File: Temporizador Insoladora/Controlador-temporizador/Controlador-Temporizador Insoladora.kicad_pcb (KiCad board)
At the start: 2 copper layers, 170.2 x 96.5 mm, 72 parts, among them P1 ICSP, P2 CONN_01X03, P3 CARGA, P4 TRANSF, P5 VAC, P7 CONN_02X08, Q1 BC548, Q2 BC548, Q3 BC548, Q4 BC548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

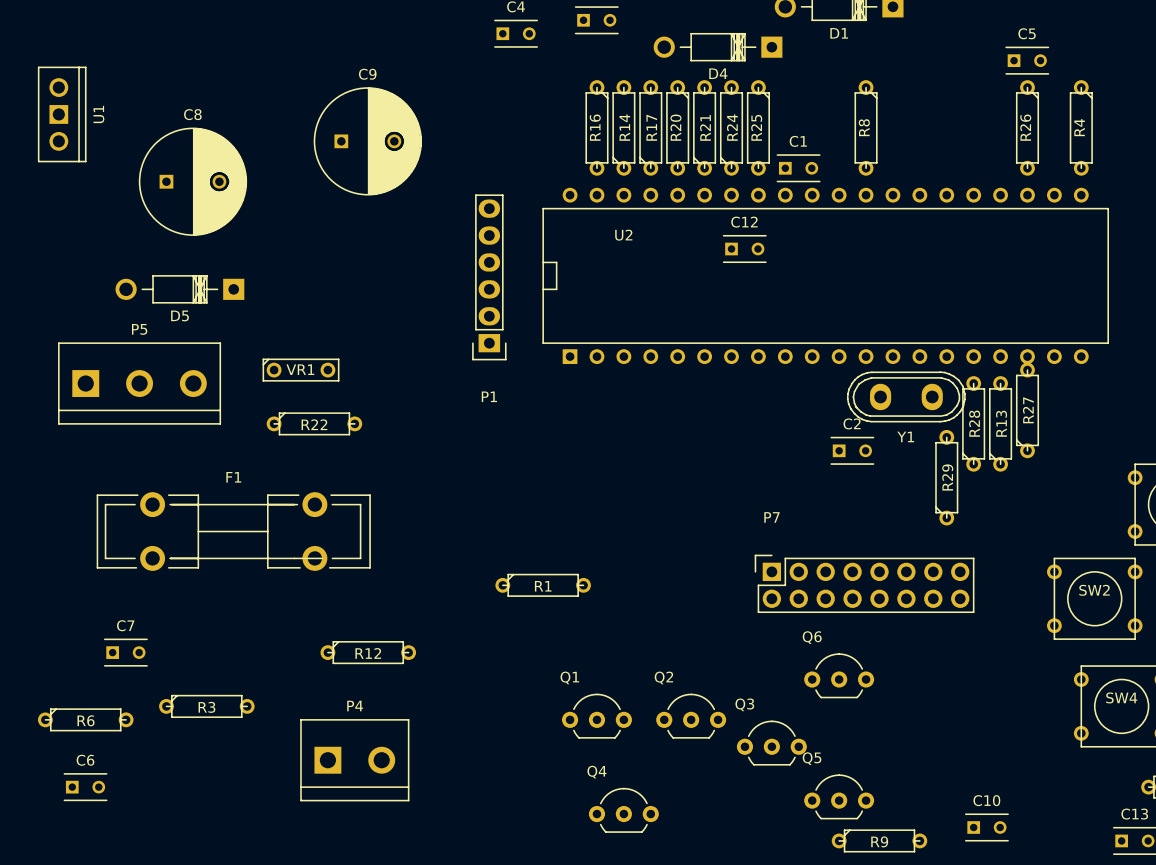
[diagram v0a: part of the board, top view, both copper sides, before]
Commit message: Comienzo a diseñar el controlador
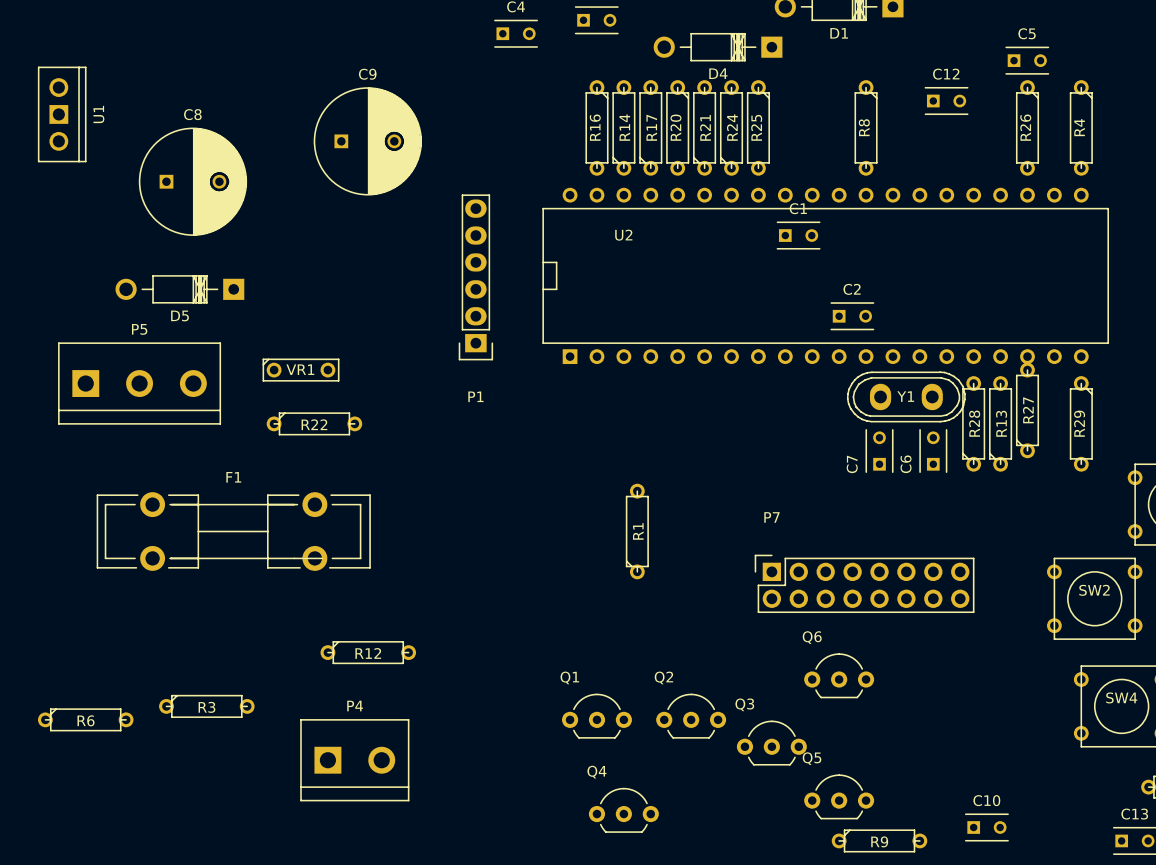
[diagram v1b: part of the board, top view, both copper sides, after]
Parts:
- moved C6 86.8 mm to (143.5, 81.3), turned to 90 degrees
- moved C7 74.5 mm to (138.4, 81.3), turned to 90 degrees
- moved C12 23.6 mm to (143.5, 47.0)
- moved R29 13.7 mm to (157.5, 77.5), turned to 270 degrees
- moved C2 12.7 mm to (134.6, 67.3)
- moved R1 10.2 mm to (115.6, 87.6), turned to 90 degrees
- moved C1 6.35 mm to (129.5, 59.7)
- moved P1 1.27 mm to (100.3, 69.8)
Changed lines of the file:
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@@
     (links 144)
     (no_connects 144)
-    (area 50.749999 22.809999 221.030001 120.315)
+    (area 38.291431 14.93 221.030001 120.315)
     (thickness 1.6)
     (drawings 6)
@@
   )
   (module Capacitors_ThroughHole:C_Rect_L4_W2.5_P2.5 (layer F.Cu)
-    (at 129.54 53.34)
+    (at 129.54 59.69)
     (descr "Film Capacitor Length 4mm x Width 2.5mm, Pitch 2.5mm")
     (tags Capacitor)
@@
   )
   (module Capacitors_ThroughHole:C_Rect_L4_W2.5_P2.5 (layer F.Cu)
-    (at 134.62 80.01)
+    (at 134.62 67.31)
     (descr "Film Capacitor Length 4mm x Width 2.5mm, Pitch 2.5mm")
     (tags Capacitor)
@@
   )
   (module Capacitors_ThroughHole:C_Rect_L4_W2.5_P2.5 (layer F.Cu)
-    (at 62.23 111.76)
+    (at 143.51 81.28 90)
     (descr "Film Capacitor Length 4mm x Width 2.5mm, Pitch 2.5mm")
     (tags Capacitor)
-    (fp_text reference C6 (at 1.25 -2.5) (layer F.SilkS)
-      (effects (font (size 1 1) (thickness 0.15)))
-    )
-    (fp_text value 20pF (at 1.25 2.5) (layer F.Fab)
+    (fp_text reference C6 (at 0 -2.54 90) (layer F.SilkS)
+      (effects (font (size 1 1) (thickness 0.15)))
+    )
+    (fp_text value 20pF (at 2.54 -2.54 90) (layer F.Fab)
       (effects (font (size 1 1) (thickness 0.15)))
     )
@@
     (fp_line (start -0.75 -1.25) (end 3.25 -1.25) (layer F.SilkS) (width 0.15))
     (fp_line (start -0.75 1.25) (end 3.25 1.25) (layer F.SilkS) (width 0.15))
-    (pad 1 thru_hole rect (at 0 0) (size 1.2 1.2) (drill 0.7) (layers *.Cu *.Mask F.SilkS)
-      (net 2 GND))
-    (pad 2 thru_hole circle (at 2.5 0) (size 1.2 1.2) (drill 0.7) (layers *.Cu *.Mask F.SilkS)
+    (pad 1 thru_hole rect (at 0 0 90) (size 1.2 1.2) (drill 0.7) (layers *.Cu *.Mask F.SilkS)
+      (net 2 GND))
+    (pad 2 thru_hole circle (at 2.5 0 90) (size 1.2 1.2) (drill 0.7) (layers *.Cu *.Mask F.SilkS)
       (net 4 "Net-(C6-Pad2)"))
   )
   (module Capacitors_ThroughHole:C_Rect_L4_W2.5_P2.5 (layer F.Cu)
-    (at 66.04 99.06)
+    (at 138.43 81.28 90)
     (descr "Film Capacitor Length 4mm x Width 2.5mm, Pitch 2.5mm")
     (tags Capacitor)
-    (fp_text reference C7 (at 1.25 -2.5) (layer F.SilkS)
-      (effects (font (size 1 1) (thickness 0.15)))
-    )
-    (fp_text value 20pF (at 1.25 2.5) (layer F.Fab)
+    (fp_text reference C7 (at 0 -2.54 90) (layer F.SilkS)
+      (effects (font (size 1 1) (thickness 0.15)))
+    )
+    (fp_text value 20pF (at 2.54 -2.54 90) (layer F.Fab)
       (effects (font (size 1 1) (thickness 0.15)))
     )
@@
     (fp_line (start -0.75 -1.25) (end 3.25 -1.25) (layer F.SilkS) (width 0.15))
     (fp_line (start -0.75 1.25) (end 3.25 1.25) (layer F.SilkS) (width 0.15))
-    (pad 1 thru_hole rect (at 0 0) (size 1.2 1.2) (drill 0.7) (layers *.Cu *.Mask F.SilkS)
-      (net 2 GND))
-    (pad 2 thru_hole circle (at 2.5 0) (size 1.2 1.2) (drill 0.7) (layers *.Cu *.Mask F.SilkS)
+    (pad 1 thru_hole rect (at 0 0 90) (size 1.2 1.2) (drill 0.7) (layers *.Cu *.Mask F.SilkS)
+      (net 2 GND))
+    (pad 2 thru_hole circle (at 2.5 0 90) (size 1.2 1.2) (drill 0.7) (layers *.Cu *.Mask F.SilkS)
       (net 5 "Net-(C7-Pad2)"))
   )
@@
   )
   (module Capacitors_ThroughHole:C_Rect_L4_W2.5_P2.5 (layer F.Cu)
-    (at 124.46 60.96)
+    (at 143.51 46.99)
     (descr "Film Capacitor Length 4mm x Width 2.5mm, Pitch 2.5mm")
     (tags Capacitor)
@@
   )
   (module Pin_Headers:Pin_Header_Straight_1x06 (layer F.Cu)
-    (at 101.6 69.85 180)
+    (at 100.33 69.85 180)
     (descr "Through hole pin header")
     (tags "pin header")
@@
   )
   (module Discret:R3 (layer F.Cu)
-    (at 106.68 92.71)
-    (descr "Resitance 3 pas")
-    (tags R)
-    (fp_text reference R1 (at 0 0.127) (layer F.SilkS)
-      (effects (font (size 1 1) (thickness 0.15)))
-    )
-    (fp_text value 10k (at 0 0.127) (layer F.Fab)
-      (effects (font (size 1 1) (thickness 0.15)))
-    )
-    (fp_line (start -3.81 0) (end -3.302 0) (layer F.SilkS) (width 0.15))
-    (fp_line (start 3.81 0) (end 3.302 0) (layer F.SilkS) (width 0.15))
-    (fp_line (start 3.302 0) (end 3.302 -1.016) (layer F.SilkS) (width 0.15))
-    (fp_line (start 3.302 -1.016) (end -3.302 -1.016) (layer F.SilkS) (width 0.15))
-    (fp_line (start -3.302 -1.016) (end -3.302 1.016) (layer F.SilkS) (width 0.15))
-    (fp_line (start -3.302 1.016) (end 3.302 1.016) (layer F.SilkS) (width 0.15))
-    (fp_line (start 3.302 1.016) (end 3.302 0) (layer F.SilkS) (width 0.15))
-    (fp_line (start -3.302 -0.508) (end -2.794 -1.016) (layer F.SilkS) (width 0.15))
-    (pad 1 thru_hole circle (at -3.81 0) (size 1.397 1.397) (drill 0.8128) (layers *.Cu *.Mask F.SilkS)
+    (at 115.57 87.63 90)
+    (descr "Resitance 3 pas")
+    (tags R)
+    (fp_text reference R1 (at 0 0.127 90) (layer F.SilkS)
+      (effects (font (size 1 1) (thickness 0.15)))
+    )
+    (fp_text value 10k (at 0 0.127 90) (layer F.Fab)
+      (effects (font (size 1 1) (thickness 0.15)))
+    )
+    (fp_line (start -3.81 0) (end -3.302 0) (layer F.SilkS) (width 0.15))
+    (fp_line (start 3.81 0) (end 3.302 0) (layer F.SilkS) (width 0.15))
+    (fp_line (start 3.302 0) (end 3.302 -1.016) (layer F.SilkS) (width 0.15))
+    (fp_line (start 3.302 -1.016) (end -3.302 -1.016) (layer F.SilkS) (width 0.15))
+    (fp_line (start -3.302 -1.016) (end -3.302 1.016) (layer F.SilkS) (width 0.15))
+    (fp_line (start -3.302 1.016) (end 3.302 1.016) (layer F.SilkS) (width 0.15))
+    (fp_line (start 3.302 1.016) (end 3.302 0) (layer F.SilkS) (width 0.15))
+    (fp_line (start -3.302 -0.508) (end -2.794 -1.016) (layer F.SilkS) (width 0.15))
+    (pad 1 thru_hole circle (at -3.81 0 90) (size 1.397 1.397) (drill 0.8128) (layers *.Cu *.Mask F.SilkS)
       (net 1 VCC))
-    (pad 2 thru_hole circle (at 3.81 0) (size 1.397 1.397) (drill 0.8128) (layers *.Cu *.Mask F.SilkS)
+    (pad 2 thru_hole circle (at 3.81 0 90) (size 1.397 1.397) (drill 0.8128) (layers *.Cu *.Mask F.SilkS)
       (net 3 "Net-(C4-Pad1)"))
     (model Discret.3dshapes/R3.wrl
@@
   )
   (module Discret:R3 (layer F.Cu)
-    (at 144.78 82.55 90)
-    (descr "Resitance 3 pas")
-    (tags R)
-    (fp_text reference R29 (at 0 0.127 90) (layer F.SilkS)
-      (effects (font (size 1 1) (thickness 0.15)))
-    )
-    (fp_text value 10K (at 0 0.127 90) (layer F.Fab)
-      (effects (font (size 1 1) (thickness 0.15)))
-    )
-    (fp_line (start -3.81 0) (end -3.302 0) (layer F.SilkS) (width 0.15))
-    (fp_line (start 3.81 0) (end 3.302 0) (layer F.SilkS) (width 0.15))
-    (fp_line (start 3.302 0) (end 3.302 -1.016) (layer F.SilkS) (width 0.15))
-    (fp_line (start 3.302 -1.016) (end -3.302 -1.016) (layer F.SilkS) (width 0.15))
-    (fp_line (start -3.302 -1.016) (end -3.302 1.016) (layer F.SilkS) (width 0.15))
-    (fp_line (start -3.302 1.016) (end 3.302 1.016) (layer F.SilkS) (width 0.15))
-    (fp_line (start 3.302 1.016) (end 3.302 0) (layer F.SilkS) (width 0.15))
-    (fp_line (start -3.302 -0.508) (end -2.794 -1.016) (layer F.SilkS) (width 0.15))
-    (pad 1 thru_hole circle (at -3.81 0 90) (size 1.397 1.397) (drill 0.8128) (layers *.Cu *.Mask F.SilkS)
+    (at 157.48 77.47 270)
+    (descr "Resitance 3 pas")
+    (tags R)
+    (fp_text reference R29 (at 0 0.127 270) (layer F.SilkS)
+      (effects (font (size 1 1) (thickness 0.15)))
+    )
+    (fp_text value 10K (at 0 0.127 270) (layer F.Fab)
+      (effects (font (size 1 1) (thickness 0.15)))
+    )
+    (fp_line (start -3.81 0) (end -3.302 0) (layer F.SilkS) (width 0.15))
+    (fp_line (start 3.81 0) (end 3.302 0) (layer F.SilkS) (width 0.15))
+    (fp_line (start 3.302 0) (end 3.302 -1.016) (layer F.SilkS) (width 0.15))
+    (fp_line (start 3.302 -1.016) (end -3.302 -1.016) (layer F.SilkS) (width 0.15))
+    (fp_line (start -3.302 -1.016) (end -3.302 1.016) (layer F.SilkS) (width 0.15))
+    (fp_line (start -3.302 1.016) (end 3.302 1.016) (layer F.SilkS) (width 0.15))
+    (fp_line (start 3.302 1.016) (end 3.302 0) (layer F.SilkS) (width 0.15))
+    (fp_line (start -3.302 -0.508) (end -2.794 -1.016) (layer F.SilkS) (width 0.15))
+    (pad 1 thru_hole circle (at -3.81 0 270) (size 1.397 1.397) (drill 0.8128) (layers *.Cu *.Mask F.SilkS)
       (net 47 "Net-(Q6-Pad2)"))
-    (pad 2 thru_hole circle (at 3.81 0 90) (size 1.397 1.397) (drill 0.8128) (layers *.Cu *.Mask F.SilkS)
+    (pad 2 thru_hole circle (at 3.81 0 270) (size 1.397 1.397) (drill 0.8128) (layers *.Cu *.Mask F.SilkS)
       (net 67 SEGU))
     (model Discret.3dshapes/R3.wrl
@@
     (descr "Crystal, Quarz, HC50/U, vertical, stehend,")
     (tags "Crystal, Quarz, HC50/U, vertical, stehend,")
-    (fp_text reference Y1 (at 0 -3.81 180) (layer F.SilkS)
-      (effects (font (size 1 1) (thickness 0.15)))
-    )
-    (fp_text value Crystal_Small (at 0 3.81 180) (layer F.Fab)
-      (effects (font (size 1 1) (thickness 0.15)))
-    )
+    (fp_text reference Y1 (at 0 0 180) (layer F.SilkS)
+      (effects (font (size 1 1) (thickness 0.15)))
+    )
+    (fp_text value Crystal_Small (at 0 2.54 180) (layer F.Fab) hide
+      (effects (font (size 1 1) (thickness 0.15)))
+    )

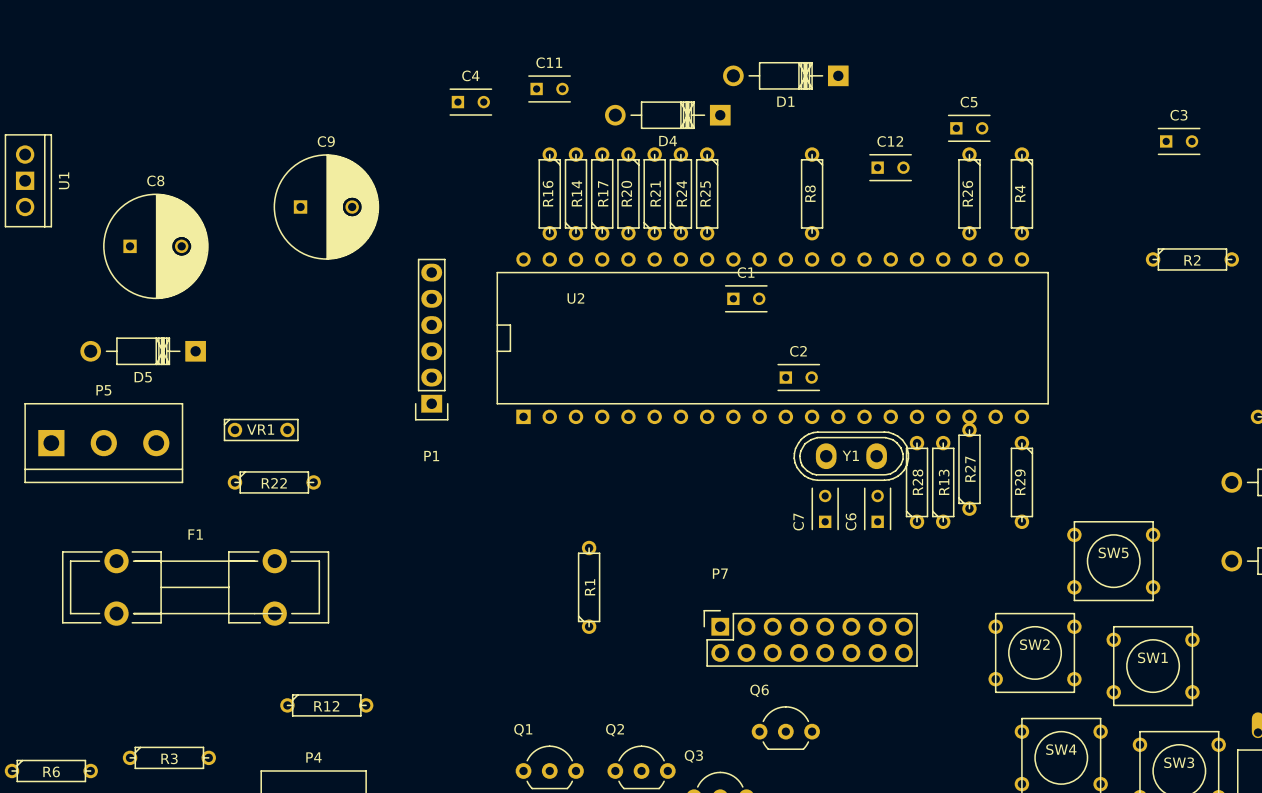
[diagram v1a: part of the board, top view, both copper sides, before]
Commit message: Comienzo ruteo controlador insoladora
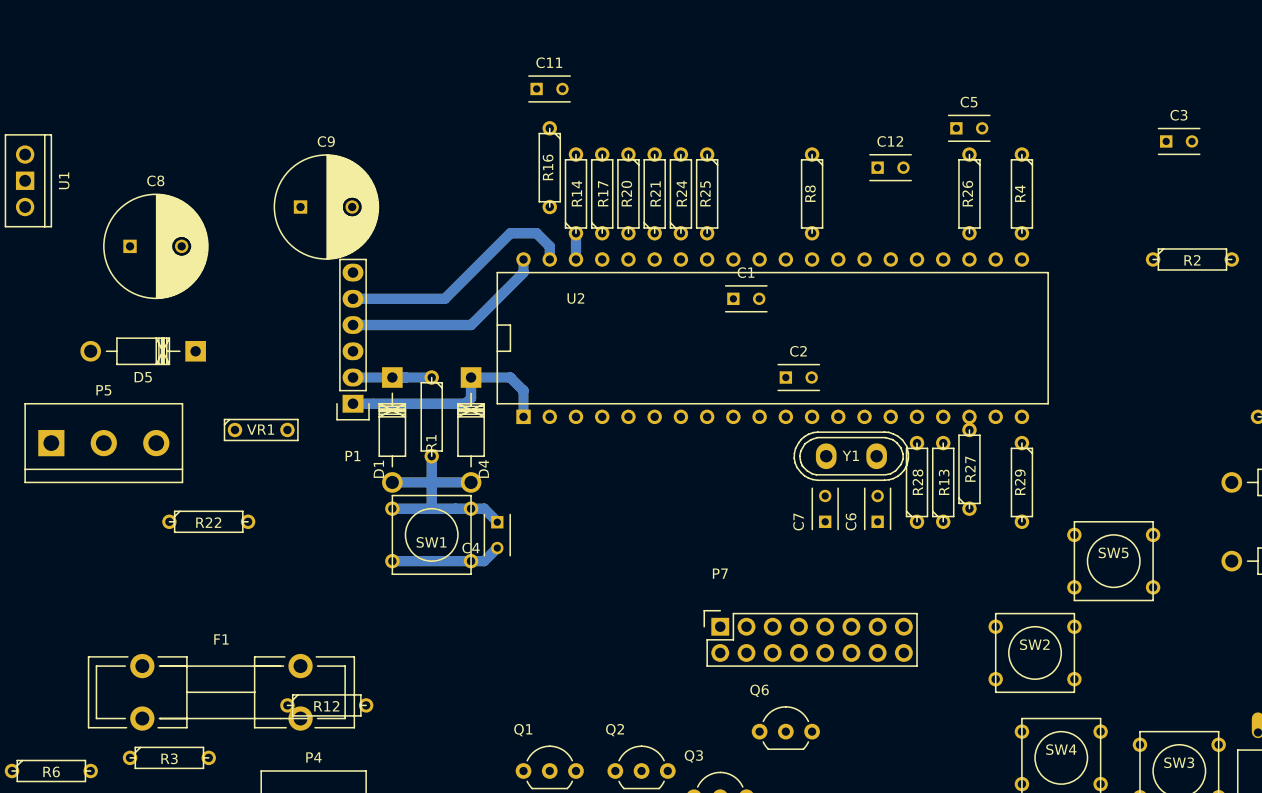
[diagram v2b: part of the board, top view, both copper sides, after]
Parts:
- moved SW1 71.0 mm to (100.3, 82.5), turned to 180 degrees
- moved D1 51.3 mm to (96.5, 72.4), turned to 90 degrees
- moved C4 40.9 mm to (106.7, 81.3), turned to 270 degrees
- moved D4 35.9 mm to (104.1, 72.4), turned to 90 degrees
- moved R1 22.5 mm to (100.3, 71.1), turned to 270 degrees
- moved F1 10.5 mm to (80.0, 97.8)
- moved P1 7.62 mm to (92.7, 69.8)
- moved R22 7.41 mm to (78.7, 81.3)
- moved R16 2.54 mm to (111.8, 47.0)
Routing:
- net PGC: track 0.00 -> 23.5 mm
- net Net-(C4-Pad1): track 0.00 -> 23.2 mm
- net ~MCLR~/VPP: track 0.00 -> 21.8 mm
- net PGD: track 0.00 -> 19.9 mm
- net GND: track 0.00 -> 10.7 mm
- net VCC: track 0.00 -> 7.62 mm
- net SUBIR: track 0.00 -> 2.54 mm
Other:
- net class Default: clearance 0.2 -> 0.7; trace_width 0.25 -> 1; via_dia 0.6 -> 1.5; via_drill 0.4 -> 0.7
- rule trace_clearance: 0.2 -> 0.7

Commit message: Sigo ruteando pcb controlador insoladora
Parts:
- moved C14 131.4 mm to (80.0, 73.7)
- moved R6 105.4 mm to (168.9, 104.1), turned to 180 degrees
- moved R10 98.8 mm to (127.0, 135.9)
- moved R11 91.1 mm to (125.7, 141.0)
- moved SW3 88.0 mm to (90.2, 74.9)
- moved C3 78.9 mm to (95.2, 64.8)
- moved R3 70.6 mm to (144.8, 114.3), turned to 90 degrees
- moved Q4 67.1 mm to (175.3, 92.7), turned to 180 degrees
- moved C10 61.0 mm to (95.2, 83.8)
- moved SW2 59.1 mm to (105.4, 68.6)
- moved C12 58.6 mm to (87.6, 64.8)
- moved Q3 55.1 mm to (175.3, 83.8), turned to 180 degrees
- moved P7 53.4 mm to (181.6, 94.0), turned to 270 degrees
- moved SW5 51.8 mm to (116.8, 69.8)
- moved P4 51.2 mm to (53.3, 146.1)
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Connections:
- P1 pad 6: Net-(P1-Pad6) -> (no net)
- P5 pad 2: Earth -> (no net)
- P7 pad 11: Net-(P7-Pad11) -> (no net)
- P7 pad 5: Net-(P7-Pad5) -> (no net)
- P7 pad 7: Net-(P7-Pad7) -> (no net)
- P7 pad 9: Net-(P7-Pad9) -> (no net)
- Q1 pad 1: MINDKC -> Net-(Q1-Pad1)
- Q3 pad 1: Net-(Q3-Pad1) -> MINDKC
- R13 pad 1: Net-(Q3-Pad2) -> Net-(Q1-Pad2)
- R15 pad 2: Net-(Q3-Pad1) -> Net-(Q1-Pad1)
- R26 pad 1: Net-(Q1-Pad2) -> Net-(Q3-Pad2)
- U2 pad 10: Net-(U2-Pad10) -> (no net)
- U2 pad 2: Net-(U2-Pad2) -> (no net)
- U2 pad 24: Net-(U2-Pad24) -> (no net)
- U2 pad 25: Net-(U2-Pad25) -> (no net)
- U2 pad 26: Net-(U2-Pad26) -> (no net)
- U2 pad 3: Net-(U2-Pad3) -> (no net)
- U2 pad 34: Net-(U2-Pad34) -> (no net)
- U2 pad 4: Net-(U2-Pad4) -> (no net)
- U2 pad 5: Net-(U2-Pad5) -> (no net)
- U2 pad 6: Net-(U2-Pad6) -> (no net)
- U2 pad 7: Net-(U2-Pad7) -> (no net)
- U2 pad 8: Net-(U2-Pad8) -> (no net)
- U2 pad 9: Net-(U2-Pad9) -> (no net)
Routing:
- net /RD4: track 0.00 -> 59.5 mm
- net MINU: track 0.00 -> 51.5 mm
- net /RD7: track 0.00 -> 42.4 mm
- net SEGU: track 0.00 -> 41.5 mm
- net SEGD: track 0.00 -> 30.7 mm
- net MIND: track 0.00 -> 27.2 mm
- net /RD2: track 0.00 -> 17.3 mm
- net MINDKC: track 0.00 -> 11.7 mm
- net SEGUKC: track 0.00 -> 10.5 mm
- net /C: track 0.00 -> 10.2 mm
- net /DP: track 0.00 -> 8.89 mm
- net /D: track 0.00 -> 8.89 mm
- net Net-(C7-Pad2): track 0.00 -> 8.19 mm
- net Net-(C6-Pad2): track 0.00 -> 8.19 mm
- net MINUKC: track 0.00 -> 6.88 mm
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
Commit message: Sigo ruteando pcb controlador insoladora
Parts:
- moved Q1 79.0 mm to (146.1, 78.7)
- moved R13 28.1 mm to (142.2, 86.4), turned to 270 degrees
- moved R5 9.92 mm to (158.8, 100.3), turned to 90 degrees
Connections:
- P1 pad 6: (no net) -> Net-(P1-Pad6)
- P5 pad 2: (no net) -> Earth
- P7 pad 11: (no net) -> Net-(P7-Pad11)
- P7 pad 5: (no net) -> Net-(P7-Pad5)
- P7 pad 7: (no net) -> Net-(P7-Pad7)
- P7 pad 9: (no net) -> Net-(P7-Pad9)
- U2 pad 10: (no net) -> Net-(U2-Pad10)
- U2 pad 15: SALIDAOPTO -> SEGU
- U2 pad 16: SEGU -> SEGD
- U2 pad 17: SEGD -> MINU
- U2 pad 18: MINU -> MIND
- U2 pad 2: (no net) -> Net-(U2-Pad2)
- U2 pad 23: MIND -> SALIDAOPTO
- U2 pad 24: (no net) -> Net-(U2-Pad24)
- U2 pad 25: (no net) -> Net-(U2-Pad25)
- U2 pad 26: (no net) -> Net-(U2-Pad26)
- U2 pad 3: (no net) -> Net-(U2-Pad3)
- U2 pad 34: (no net) -> Net-(U2-Pad34)
- U2 pad 4: (no net) -> Net-(U2-Pad4)
- U2 pad 5: (no net) -> Net-(U2-Pad5)
- U2 pad 6: (no net) -> Net-(U2-Pad6)
- U2 pad 7: (no net) -> Net-(U2-Pad7)
- U2 pad 8: (no net) -> Net-(U2-Pad8)
- U2 pad 9: (no net) -> Net-(U2-Pad9)
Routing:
- net MINU: track 51.5 -> 0.00 mm
- net SEGU: track 41.5 -> 0.00 mm
- net SEGD: track 30.7 -> 0.00 mm
- net MIND: track 27.2 -> 0.00 mm
- net /RD3: track 0.00 -> 18.4 mm
- net /D: track 8.89 -> 22.1 mm
- net /RD6: track 0.00 -> 2.54 mm

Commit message: Sigo ruteando controlador
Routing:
- net /RD4: track 59.5 -> 0.00 mm
- net /RD7: track 42.4 -> 0.00 mm
- net /RD3: track 18.4 -> 0.00 mm
- net /RD2: track 17.3 -> 0.00 mm
